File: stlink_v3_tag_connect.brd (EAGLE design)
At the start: 39.2 x 49.9 mm, 10 parts, among them CON1 STLINK_V3_HAT_SWD/JTAG_MINIMAL, J1 RJ12, U1 SN74LVC2T45DCU

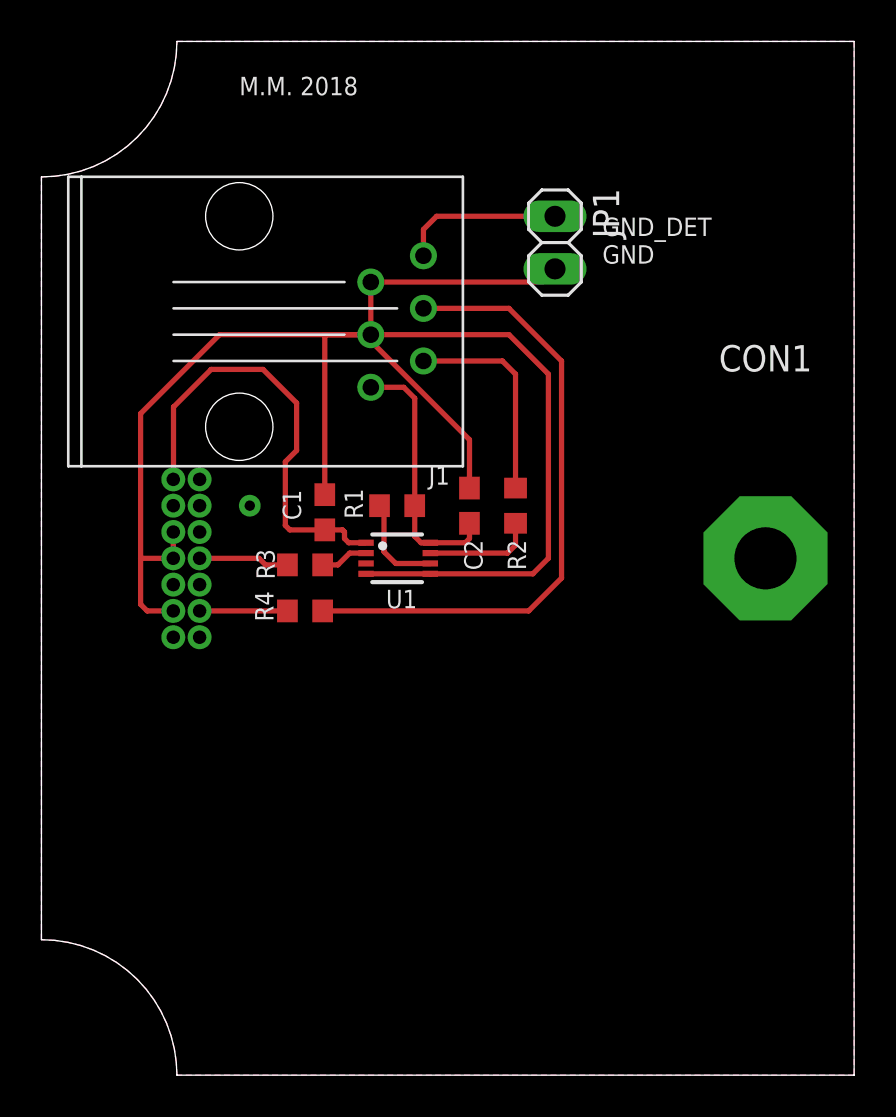
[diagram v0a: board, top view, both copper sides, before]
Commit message: Fix missing SWIM data line back to the StLink
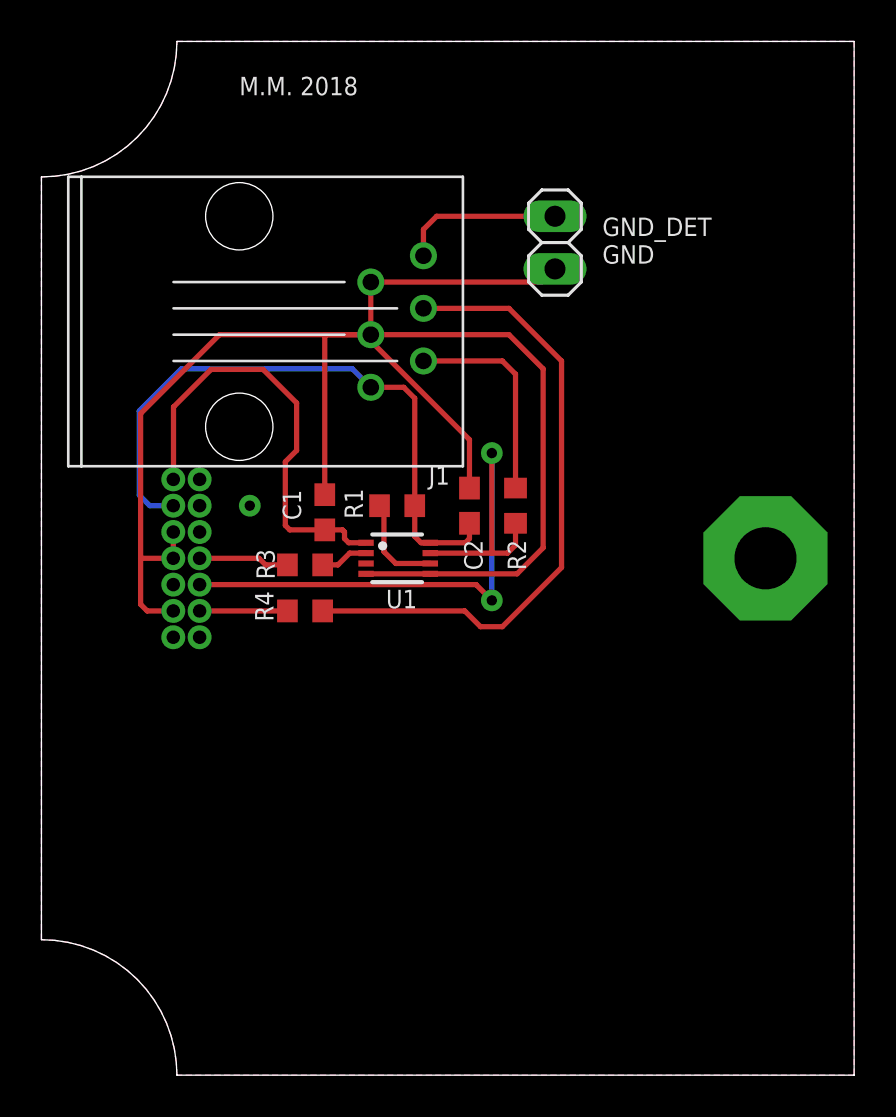
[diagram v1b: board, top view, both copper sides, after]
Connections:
- removed net VCC_TARGET: C2.1, J1.6, R1.2, U1.8
- net SWIM_TARGET_R: now also CON1.STDC_14_10
- net TARGET_VCC: now also C2.1, J1.6, R1.2, U1.8
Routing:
- net TARGET_VCC: track 0.00 -> 30.9 mm
- net SWIM_TARGET_R: track 5.33 -> 31.7 mm, vias 0 -> 2
- net VCC_TARGET: track 12.6 -> 0.00 mm
- net GND: track 84.8 -> 84.2 mm

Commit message: Sch prettify
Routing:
- net TARGET_VCC: track 30.9 -> 30.0 mm
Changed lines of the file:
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@@
 <layer number="101" name="Patch_Top" color="12" fill="4" visible="no" active="yes"/>
 <layer number="102" name="Vscore" color="7" fill="1" visible="no" active="yes"/>
-<layer number="103" name="ATT_MISO" color="7" fill="1" visible="yes" active="yes"/>
+<layer number="103" name="ATT_MISO" color="7" fill="1" visible="no" active="yes"/>
 <layer number="104" name="Name" color="7" fill="1" visible="no" active="yes"/>
-<layer number="105" name="Beschreib" color="7" fill="1" visible="yes" active="yes"/>
-<layer number="106" name="BGA-Top" color="7" fill="1" visible="yes" active="yes"/>
-<layer number="107" name="BD-Top" color="7" fill="1" visible="yes" active="yes"/>
-<layer number="108" name="centerline" color="7" fill="1" visible="yes" active="yes"/>
+<layer number="105" name="Beschreib" color="7" fill="1" visible="no" active="yes"/>
+<layer number="106" name="BGA-Top" color="7" fill="1" visible="no" active="yes"/>
+<layer number="107" name="BD-Top" color="7" fill="1" visible="no" active="yes"/>
+<layer number="108" name="centerline" color="7" fill="1" visible="no" active="yes"/>
 <layer number="116" name="Patch_BOT" color="9" fill="4" visible="no" active="yes"/>
 <layer number="121" name="_tsilk" color="7" fill="1" visible="no" active="yes"/>
 <layer number="122" name="_bsilk" color="7" fill="1" visible="no" active="yes"/>
 <layer number="126" name="_bNames" color="5" fill="1" visible="no" active="yes"/>
-<layer number="131" name="prix" color="7" fill="1" visible="yes" active="yes"/>
-<layer number="132" name="test" color="7" fill="1" visible="yes" active="yes"/>
+<layer number="131" name="prix" color="7" fill="1" visible="no" active="yes"/>
+<layer number="132" name="test" color="7" fill="1" visible="no" active="yes"/>
 <layer number="151" name="HeatSink" color="7" fill="1" visible="no" active="yes"/>
 <layer number="200" name="200bmp" color="1" fill="10" visible="no" active="no"/>
@@
 <wire x1="-16.625" y1="0.75" x2="-16.93" y2="1.055" width="0.254" layer="1"/>
 <wire x1="-16.93" y1="1.055" x2="-16.93" y2="2.54" width="0.254" layer="1"/>
-<wire x1="-16.93" y1="2.54" x2="-16.93" y2="7.7225" width="0.254" layer="1"/>
-<wire x1="-16.93" y1="7.7225" x2="-17.4625" y2="8.255" width="0.254" layer="1"/>
-<wire x1="-17.4625" y1="8.255" x2="-19.05" y2="8.255" width="0.254" layer="1"/>
 <wire x1="-16.18" y1="0.75" x2="-14.49" y2="0.75" width="0.254" layer="1"/>
 <wire x1="-14.49" y1="0.75" x2="-14.2875" y2="0.9525" width="0.254" layer="1"/>
@@
 <wire x1="-19.939" y1="9.144" x2="-19.05" y2="8.255" width="0.254" layer="16"/>
 <wire x1="-28.194" y1="9.144" x2="-19.939" y2="9.144" width="0.254" layer="16"/>
+<wire x1="-16.93" y1="2.54" x2="-16.93" y2="6.135" width="0.254" layer="1"/>
+<wire x1="-16.93" y1="6.135" x2="-19.05" y2="8.255" width="0.254" layer="1"/>
 </signal>
 </signals>
